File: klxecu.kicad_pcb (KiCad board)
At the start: 2 copper layers, 65 parts, among them IC1 SP721, J1 Conn_02x20_Odd_Even, J2 Conn_02x18_Odd_Even, J3 Conn_02x16_Odd_Even, J4 Conn_01x01_Male, Q1 2N3904, Q2 STP62NS04Z, Q3 STP62NS04Z, Q4 STP62NS04Z, Q5 STP62NS04Z, Q6 STP62NS04Z, Q7 STP62NS04Z, U1 ERZ-V14D220, U2 LM340T-5.0, U3 MAX9924UAUB+, U4 ATtiny84-20P, U5 74LS14DR, U6 TC4422AVPA

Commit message: v1?
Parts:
- removed RN1: 470, Resistor_THT:R_Array_SIP12
- added R16: 470, Resistor_SMD:R_0805_2012Metric_Pad1.20x1.40mm_HandSolder, F.Cu at (132.1, 55.9)
- added R17: 470, Resistor_SMD:R_0805_2012Metric_Pad1.20x1.40mm_HandSolder, F.Cu at (132.1, 53.3)
- added R18: 470, Resistor_SMD:R_0805_2012Metric_Pad1.20x1.40mm_HandSolder, F.Cu at (135.9, 47.0)
- added R19: 470, Resistor_SMD:R_0805_2012Metric_Pad1.20x1.40mm_HandSolder, F.Cu at (138.4, 47.0)
- added R20: 470, Resistor_SMD:R_0805_2012Metric_Pad1.20x1.40mm_HandSolder, F.Cu at (142.2, 55.9)
- added R21: 470, Resistor_SMD:R_0805_2012Metric_Pad1.20x1.40mm_HandSolder, F.Cu at (142.2, 53.3)
- C11, C12, C13, C17, C18, C19, C24, R13: moved to B.Cu
- moved J4 215.3 mm to (36.8, 45.7)
- moved R10 201.5 mm to (36.8, 41.9), turned to 90 degrees
- moved R12 197.4 mm to (52.1, 61.0), turned to -90 degrees
- moved R13 191.6 mm to (52.2, 61.0), turned to 90 degrees
- moved Q1 190.1 mm to (40.6, 43.2), turned to -90 degrees
- moved Q6 186.1 mm to (51.5, 80.3)
- moved C24 158.9 mm to (54.7, 61.0), turned to 90 degrees
- moved JP1 145.1 mm to (72.4, 36.8), turned to 180 degrees
- moved R11 135.0 mm to (108.0, 73.7), turned to 180 degrees
- moved C7 122.5 mm to (132.1, 58.4)
- moved R7 115.9 mm to (133.3, 43.2), turned to -90 degrees
- moved C8 111.7 mm to (132.1, 50.8)
- moved R6 110.0 mm to (133.3, 47.0), turned to -90 degrees
- moved C15 107.8 mm to (142.2, 58.4), turned to 180 degrees
- moved C9 107.4 mm to (135.9, 43.2), turned to 90 degrees
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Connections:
- RN3 pad 11: ARDUINO-D30 -> ATTINY-D10
- RN3 pad 12: Net-(Q4-Pad1) -> Net-(Q5-Pad1)
- RN3 pad 7: ATTINY-D10 -> ARDUINO-D30
- RN3 pad 8: Net-(Q5-Pad1) -> Net-(Q4-Pad1)
- U5 pad 10: (no net) -> unconnected-(U5-Pad10)
- U5 pad 11: (no net) -> GND
- U5 pad 12: (no net) -> unconnected-(U5-Pad12)
- U5 pad 13: (no net) -> +5V
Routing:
- net GND: track 231.6 -> 641.1 mm, vias 0 -> 1
- net +5V: track 107.2 -> 323.2 mm, vias 4 -> 6
- net O2S +: track 12.5 -> 149.1 mm, vias 0 -> 2
- net CLT: track 15.0 -> 146.8 mm, vias 0 -> 2
- net CLUTCH SW: track 28.4 -> 153.1 mm
- net Net-(Q1-Pad2): track 0.00 -> 121.1 mm, vias 0 -> 1
- net MAP: track 12.0 -> 132.6 mm, vias 0 -> 2
- net +12V: track 27.4 -> 138.1 mm
- net IAT: track 19.1 -> 128.6 mm, vias 0 -> 2
- net TPS: track 11.4 -> 119.4 mm, vias 0 -> 2
- net ARDUINO-D19: track 8.80 -> 104.4 mm
- net ARDUINO-D42: track 0.00 -> 89.9 mm
- net ARDUINO-D32: track 0.00 -> 89.4 mm, vias 0 -> 1
- net ATTINY-D10: track 0.00 -> 87.0 mm, vias 0 -> 2
- net ARDUINO-D23: track 0.00 -> 86.0 mm
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
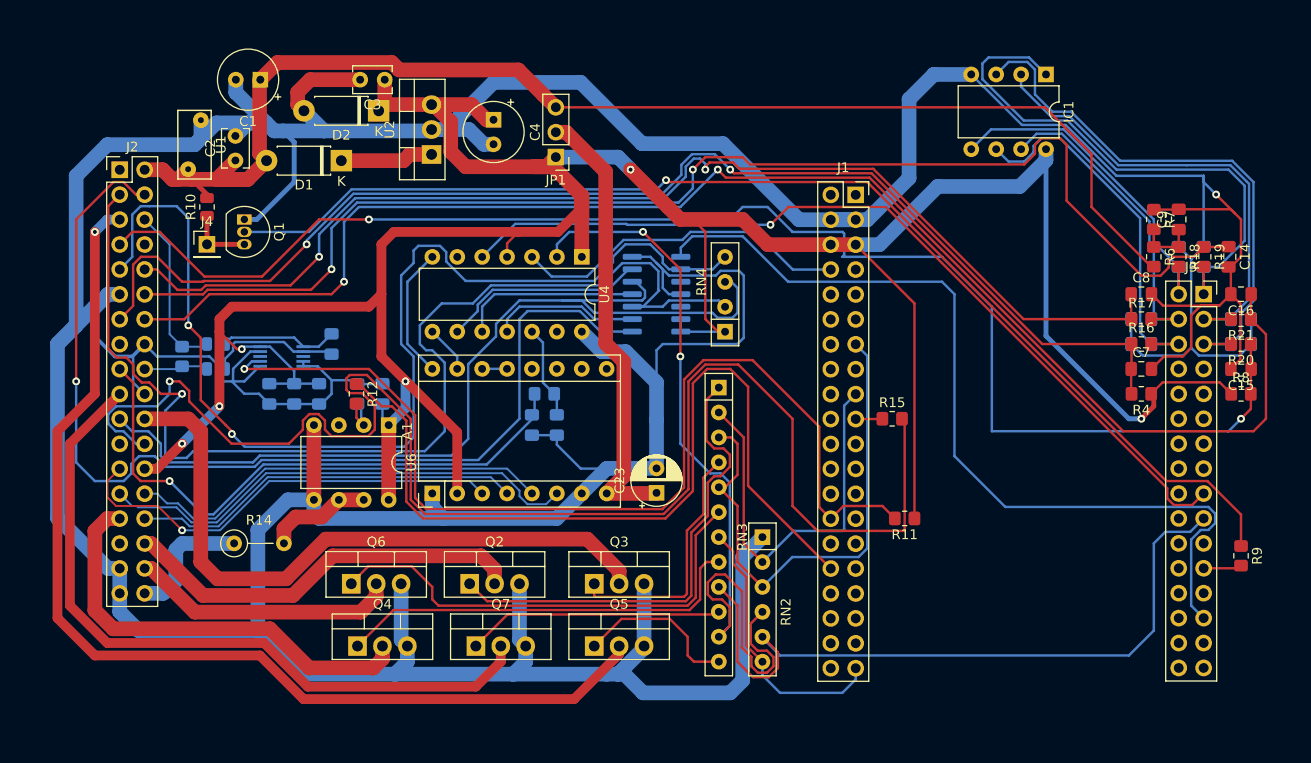
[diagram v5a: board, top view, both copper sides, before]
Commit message: Fix up board, add copper fills
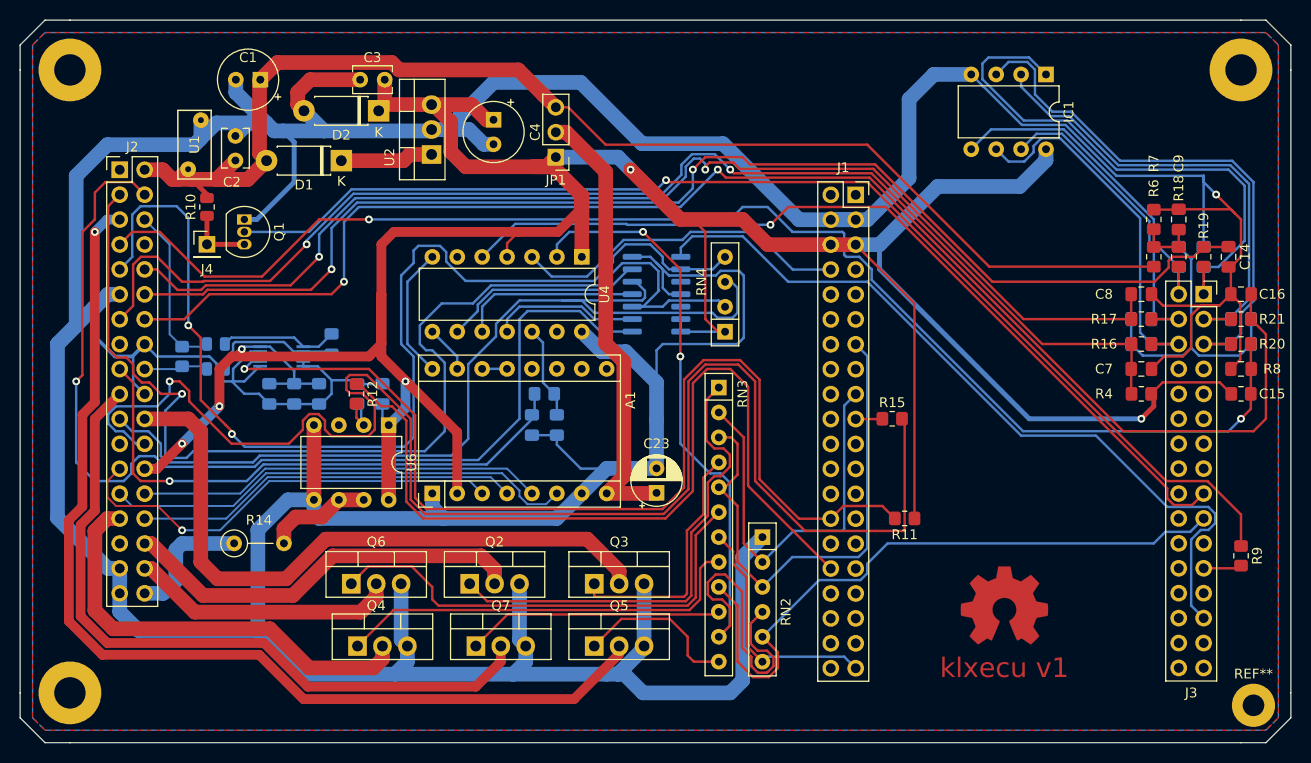
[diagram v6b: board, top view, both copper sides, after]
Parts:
- added ?: , , F.Cu at (142.2, 27.9)
- added ?: , , F.Cu at (22.9, 91.4)
- added ?: , , F.Cu at (22.9, 27.9)
- added REF**: OSHW-Symbol_8.9x8mm_Copper, Symbol:OSHW-Symbol_8.9x8mm_Copper, F.Cu at (118.1, 82.5)
- added REF**: MountingHole_2.2mm_M2_Pad, MountingHole:MountingHole_2.2mm_M2_Pad, F.Cu at (143.5, 92.7)
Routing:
- net ARDUINO-D42: track 89.9 -> 80.2 mm
- net CLT: track 146.8 -> 139.6 mm
- net ARDUINO-D34: track 74.2 -> 68.0 mm
- net MAP: track 132.6 -> 127.0 mm
- net +12V: track 138.1 -> 133.1 mm
- net +5V: track 323.2 -> 326.5 mm
- net ARDUINO-D30: track 27.9 -> 24.8 mm
- net SUB TPS: track 60.3 -> 57.5 mm
- net SUB B +: track 43.7 -> 41.6 mm
- net CHECK ENGINE: track 107.4 -> 105.9 mm
- net SUB B -: track 50.0 -> 48.6 mm
- net ARDUINO-D19: track 104.4 -> 105.5 mm
- net TEMP WARN: track 73.7 -> 72.8 mm
- net CLUTCH SW: track 153.1 -> 153.8 mm
- net SUB A +: track 40.0 -> 39.4 mm
- added copper zone on B.Cu, net GND
- added copper zone on F.Cu, net GND
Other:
- board outline added: 129.5 x 73.7 mm
- board text added: "klxecu v1"
